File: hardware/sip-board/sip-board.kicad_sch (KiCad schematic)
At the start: 85 parts, among them IC1 XC7S15-1CPGA196C, J1 Conn_01x06_Pin, J2 Conn_01x10_Pin, J3 Conn_01x10_Pin, J4 Conn_01x10_Pin, J5 Conn_01x10_Pin, SW2 SW_RESET, U1 TLV75718PDRV, U2 TLV75733PDRV, U3 TLV75710PDRV

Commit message: add new spi chip supported by vivado
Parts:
- removed D1: D_Small, Diode_SMD:D_0201_0603Metric, symbol Device:D_Small
- removed J1: Conn_01x06_Pin, Connector_PinHeader_2.54mm:PinHeader_1x06_P2.54mm_Vertical_SMD_Pin1Left, symbol Connector:Conn_01x06_Pin
- removed R15: 2k4, Resistor_SMD:R_0201_0603Metric, symbol Device:R_Small
- removed SPIPROM1: M95256-WMN6P, Package_SO:SOIC-8_3.9x4.9mm_P1.27mm, symbol Memory_EEPROM:M95256-WMN6P
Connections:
- net A0_FPGA: no longer IC1.F13 (IO_L11N_T1_SRCC_14)
- net A10_FPGA: no longer IC1.N13 (IO_L20P_T3_D24_14)
- net A11_FPGA: no longer IC1.B1 (IO_L5N_T0_34)
- net A12_FPGA: no longer IC1.C1 (IO_L7N_T1_34)
- net A13_FPGA: no longer IC1.D1 (IO_L9N_T1_DQS_34)
- net A14_FPGA: no longer IC1.E1 (IO_L9P_T1_DQS_34)
- net A15_FPGA: no longer IC1.G1 (IO_L12N_T1_MRCC_34)
- net A1_FPGA: no longer IC1.F14 (IO_L12N_T1_MRCC_14)
- net A2_FPGA: no longer IC1.G14 (IO_L12P_T1_MRCC_14)
- net A3_FPGA: no longer IC1.H13 (IO_L14N_T2_SRCC_14)
- net A4_FPGA: no longer IC1.H14 (IO_L15N_T2_DQS_DOUT_CSO_B_14)
- net A5_FPGA: no longer IC1.J13 (IO_L14P_T2_SRCC_14)
- net A6_FPGA: no longer IC1.J14 (IO_L15P_T2_DQS_RDWR_B_14)
- net A7_FPGA: no longer IC1.L14 (IO_L17N_T2_D29_14)
- net A8_FPGA: no longer IC1.M14 (IO_L17P_T2_D30_14)
- net A9_FPGA: no longer IC1.N14 (IO_L20N_T3_D23_14)
- net BUSAK_FPGA: no longer IC1.C12 (IO_L5P_T0_D06_14)
- net BUSRQ_FPGA: no longer IC1.B14 (IO_L7N_T1_D10_14)
- net CLK: now also IC1.H4 (IO_L13P_T2_MRCC_34); no longer IC1.H1 (IO_L15N_T2_DQS_34)
- net D0_FPGA: no longer IC1.K3 (IO_L18P_T2_34)
- net D1_FPGA: no longer IC1.L2 (IO_L17P_T2_34)
- net D2_FPGA: no longer IC1.M1 (IO_L20N_T3_34)
- net D3_FPGA: no longer IC1.J1 (IO_L15P_T2_DQS_34)
- net D4_FPGA: no longer IC1.K1 (IO_L17N_T2_34)
- net D5_FPGA: no longer IC1.N1 (IO_L21N_T3_DQS_34)
- net D6_FPGA: no longer IC1.M2 (IO_L20P_T3_34)
- net D7_FPGA: no longer IC1.K2 (IO_L18N_T2_34)
- net DONE: no longer IC1.M9 (DONE_0)
- net HALT_FPGA: no longer IC1.N4 (IO_L24P_T3_34)
- net INT_FPGA: no longer IC1.L4 (IO_L19P_T3_34)
- net IORQ_FPGA: no longer IC1.P4 (IO_L22P_T3_34)
- net M1_FPGA: no longer IC1.D14 (IO_L8N_T1_D12_14)
- net MREQ_FPGA: no longer IC1.P3 (IO_L23P_T3_34)
- net NMI_FPGA: no longer IC1.N3 (IO_L22N_T3_34)
- net RD_FPGA: no longer IC1.A12 (IO_L2N_T0_D03_14)
- net RESET_FPGA: no longer IC1.C14 (IO_L7P_T1_D09_14)
- net RFSH_FPGA: no longer IC1.E13 (IO_L8P_T1_D11_14)
- net WAIT_FPGA: no longer IC1.A13 (IO_0_14)
- net WR_FPGA: no longer IC1.B12 (IO_L5N_T0_D07_14)
- net CCLK: no longer names the net of IC1.A7 (CCLK_0)
- net CCLK: no longer IC1.A8 (TCK_0)
- net CS: no longer names the net of IC1.D13 (IO_L6P_T0_FCS_B_14)
- net CS: no longer IC1.L7 (TMS_0)
- net DIN: no longer names the net of IC1.C11 (IO_L1N_T0_D01_DIN_14)
- net MOSI: no longer names the net of IC1.C10 (IO_L1P_T0_D00_MOSI_14)
- net MOSI: no longer IC1.M7 (TDI_0)
- net TDO: no longer names the net of IC1.M6 (TDO_0)
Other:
- note added: "Choosing is25lp016d for now; cheap, high density, qspi, directly supported by Vivado"
- note added: "M[2:0] = 001 for Master SPI config"
- note added: "`CLK` signal is routed into H4 (MRCC) as it can be used in global clock tree this must be configured in the constraints file"
- note added: "https://docs.amd.com/r/en-US/xapp586-spi-flash/SPI-Flash-Configuration-Interface https://docs.amd.com/r/2021.2-English/ug908-vivado-programming-debugging/Spartan-7-Configuration-Memory-Devices"
- note removed: "JTAG <-> SPI Thank you digilent. I love you. JTAG-HS1 Connector Note: DO NOT connect both JTAG and Z80 board at same time."
- note removed: "SPI PROM 3.9mm x 4.9mm We are configuring FPGA from SPI - see Config UG"
- moved on the sheet: J2, J3, J4, J5, R10, R11, R12, R13, R4, R5, R6, R7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

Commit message: 3d model for fpga, part placement done(?)
Look into Xilinx programming adapters still. We do not have lots of space to work with.
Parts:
- added J1: Conn_01x05_Pin, Connector_PinHeader_2.54mm:PinHeader_1x05_P2.54mm_Vertical, symbol Connector:Conn_01x05_Pin
- added U15: AT25SF081-XMHD-X, Package_SO:TSSOP-8_4.4x3mm_P0.65mm, symbol Memory_Flash:AT25SF081-XMHD-X
- C10, C12, C13, C16, C17, C18, C19, C20, C21, C22, C23, C26, C27, C28, C29, C30, C31, C32, C33, C34, C36, C37, C7, C8, C9: footprint Capacitor_SMD:C_0201_0603Metric -> Capacitor_SMD:C_01005_0402Metric
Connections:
- net +3V3: now also J1.1 (Pin_1), U15.8 (VCC)
- net A0_5V: now also J4.1 (Pin_1), U12.9 (B3); no longer J4.10 (Pin_10), U12.10 (B2)
- net A0_FPGA: now also U12.4 (A3); no longer U12.3 (A2)
- net A10_5V: now also J5.1 (Pin_1), U14.11 (B1); no longer J5.10 (Pin_10), U14.8 (B4)
- net A10_FPGA: now also U14.2 (A1); no longer U14.5 (A4)
- net A1_5V: now also J5.10 (Pin_10), U12.10 (B2); no longer J5.1 (Pin_1), U12.9 (B3)
- net A1_FPGA: now also U12.3 (A2); no longer U12.4 (A3)
- net A2_5V: now also J5.9 (Pin_9), U12.11 (B1); no longer J5.2 (Pin_2), U12.8 (B4)
- net A2_FPGA: now also U12.2 (A1); no longer U12.5 (A4)
- net A3_5V: now also J5.8 (Pin_8), U13.8 (B4); no longer J5.3 (Pin_3), U13.11 (B1)
- net A3_FPGA: now also U13.5 (A4); no longer U13.2 (A1)
- net A4_5V: now also J5.7 (Pin_7), U13.9 (B3); no longer J5.4 (Pin_4), U13.10 (B2)
- net A4_FPGA: now also U13.4 (A3); no longer U13.3 (A2)
- net A5_5V: now also J5.6 (Pin_6), U13.10 (B2); no longer J5.5 (Pin_5), U13.9 (B3)
- net A5_FPGA: now also U13.3 (A2); no longer U13.4 (A3)
- net A6_5V: now also J5.5 (Pin_5), U13.11 (B1); no longer J5.6 (Pin_6), U13.8 (B4)
- net A6_FPGA: now also U13.2 (A1); no longer U13.5 (A4)
- net A7_5V: now also J5.4 (Pin_4), U14.8 (B4); no longer J5.7 (Pin_7), U14.11 (B1)
- net A7_FPGA: now also U14.5 (A4); no longer U14.2 (A1)
- net A8_5V: now also J5.3 (Pin_3), U14.9 (B3); no longer J5.8 (Pin_8), U14.10 (B2)
- net A8_FPGA: now also U14.4 (A3); no longer U14.3 (A2)
- net A9_5V: now also J5.2 (Pin_2), U14.10 (B2); no longer J5.9 (Pin_9), U14.9 (B3)
- net A9_FPGA: now also U14.3 (A2); no longer U14.4 (A3)
- net BUSAK_5V: now also J4.8 (Pin_8), U10.10 (B2); no longer J4.3 (Pin_3), U10.9 (B3)
- net BUSAK_FPGA: now also U10.3 (A2); no longer U10.4 (A3)
- net BUSRQ_5V: now also J4.6 (Pin_6), U11.8 (B4); no longer J4.5 (Pin_5), U11.11 (B1)
- net BUSRQ_FPGA: now also U11.5 (A4); no longer U11.2 (A1)
- net DONE: now also IC1.M9 (DONE_0)
- net GND: now also J4.2 (Pin_2), U15.4 (GND); no longer J4.9 (Pin_9)
- net M1_5V: now also J4.4 (Pin_4), U11.10 (B2); no longer J4.7 (Pin_7), U11.9 (B3)
- net M1_FPGA: now also U11.3 (A2); no longer U11.4 (A3)
- net RD_5V: now also J4.10 (Pin_10), U10.8 (B4); no longer J4.1 (Pin_1), U10.11 (B1)
- net RD_FPGA: now also U10.5 (A4); no longer U10.2 (A1)
- net RESET_5V: now also J4.5 (Pin_5), U11.9 (B3); no longer J4.6 (Pin_6), U11.10 (B2)
- net RESET_FPGA: now also U11.4 (A3); no longer U11.3 (A2)
- net RFSH_5V: now also J4.3 (Pin_3), U11.11 (B1); no longer J4.8 (Pin_8), U11.8 (B4)
- net RFSH_FPGA: now also U11.2 (A1); no longer U11.5 (A4)
- net WAIT_5V: now also J4.7 (Pin_7), U10.11 (B1); no longer J4.4 (Pin_4), U10.8 (B4)
- net WAIT_FPGA: now also U10.2 (A1); no longer U10.5 (A4)
- net WR_5V: now also J4.9 (Pin_9), U10.9 (B3); no longer J4.2 (Pin_2), U10.10 (B2)
- net WR_FPGA: now also U10.4 (A3); no longer U10.3 (A2)
- net SPI_DQ3: now reaches IC1.A12 (IO_L2N_T0_D03_14)
- net SPI_DQ3: now also U15.7 (~{HOLD}/IO3)
- net SPI_SCK: now reaches IC1.A7 (CCLK_0)
- net SPI_SCK: now also U15.6 (SCK)
- net JTAG_TCK: now reaches IC1.A8 (TCK_0)
- net JTAG_TCK: now also J1.2 (Pin_2)
- net SPI_DQ2: now reaches IC1.B11 (IO_L2P_T0_D02_14)
- net SPI_DQ2: now also U15.3 (~{WP}/IO2)
- net SPI_DQ0: now reaches IC1.C10 (IO_L1P_T0_D00_MOSI_14)
- net SPI_DQ0: now also U15.5 (SI/IO0)
- net SPI_DQ1: now reaches IC1.C11 (IO_L1N_T0_D01_DIN_14)
- net SPI_DQ1: now also U15.2 (SO/IO1)
- net SPI_CS: now reaches IC1.D13 (IO_L6P_T0_FCS_B_14)
- net SPI_CS: now also U15.1 (~{CS})
- net JTAG_TMS: now reaches IC1.L7 (TMS_0)
- net JTAG_TMS: now also J1.3 (Pin_3)
- net JTAG_TDO: now reaches IC1.M6 (TDO_0)
- net JTAG_TDO: now also J1.5 (Pin_5)
- net JTAG_TDI: now reaches IC1.M7 (TDI_0)
- net JTAG_TDI: now also J1.4 (Pin_4)
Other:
- note added: "Configuration Banks Voltage Select section in the config user guide; tldr we are running of 3v3 for SPI flash so this needs to be pulled up to 3v3 as well"
- note added: "SPI Memory"
- note added: "The Xilinx connector is actually a 2x7 connector, but half the pins are ground, 4 of the pins are real JTAG signals, 1 is power, and 2 are NC."
- note added: "This A4 pin --> is GND on original Z80"
- note added: "This chip is not directly supported by Vivado for flash programming. We need to determine if it works identically to the supported chips or if we have to configure Vivado for it"
- note added: "Xilinx JTAG connector"
- note added: "Xilinx recommends specific power on sequence for each LDO, but I haven't found small enough LDOs with enable pins, so we're scaling up the capacitor values for now. Fix!"
- note removed: "Choosing is25lp016d for now; cheap, high density, qspi, directly supported by Vivado"
- note removed: "Configuration Banks Voltage Select section in the config user guide"
- note removed: "This A1 --> is GND on original Z80"

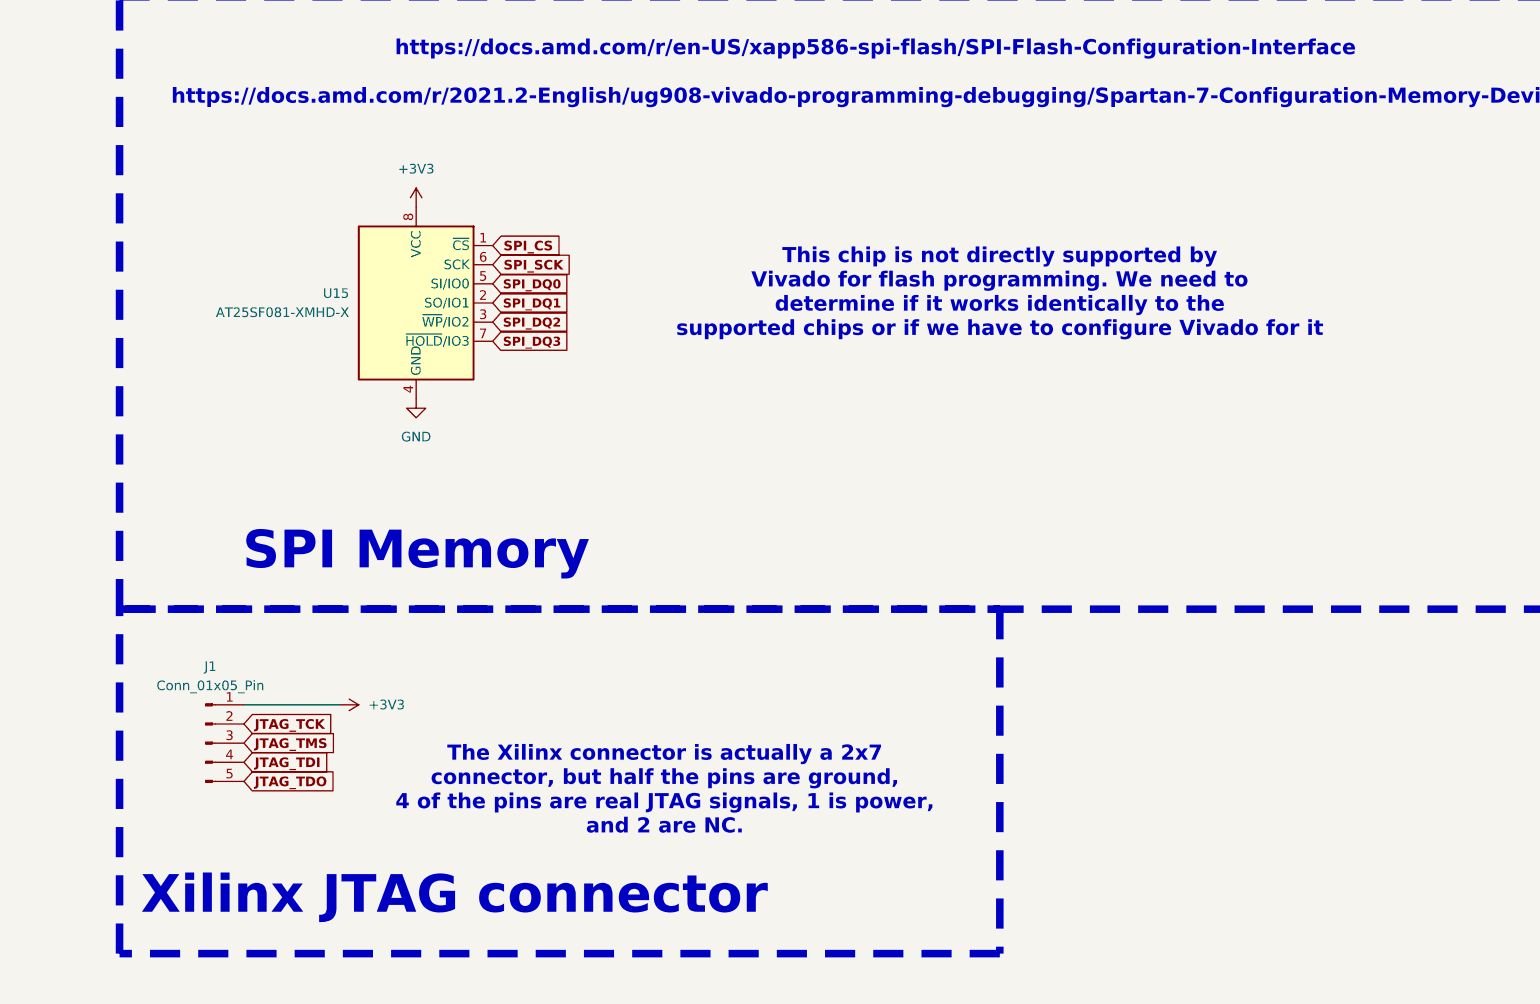
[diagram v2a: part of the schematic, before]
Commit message: update to use relative paths
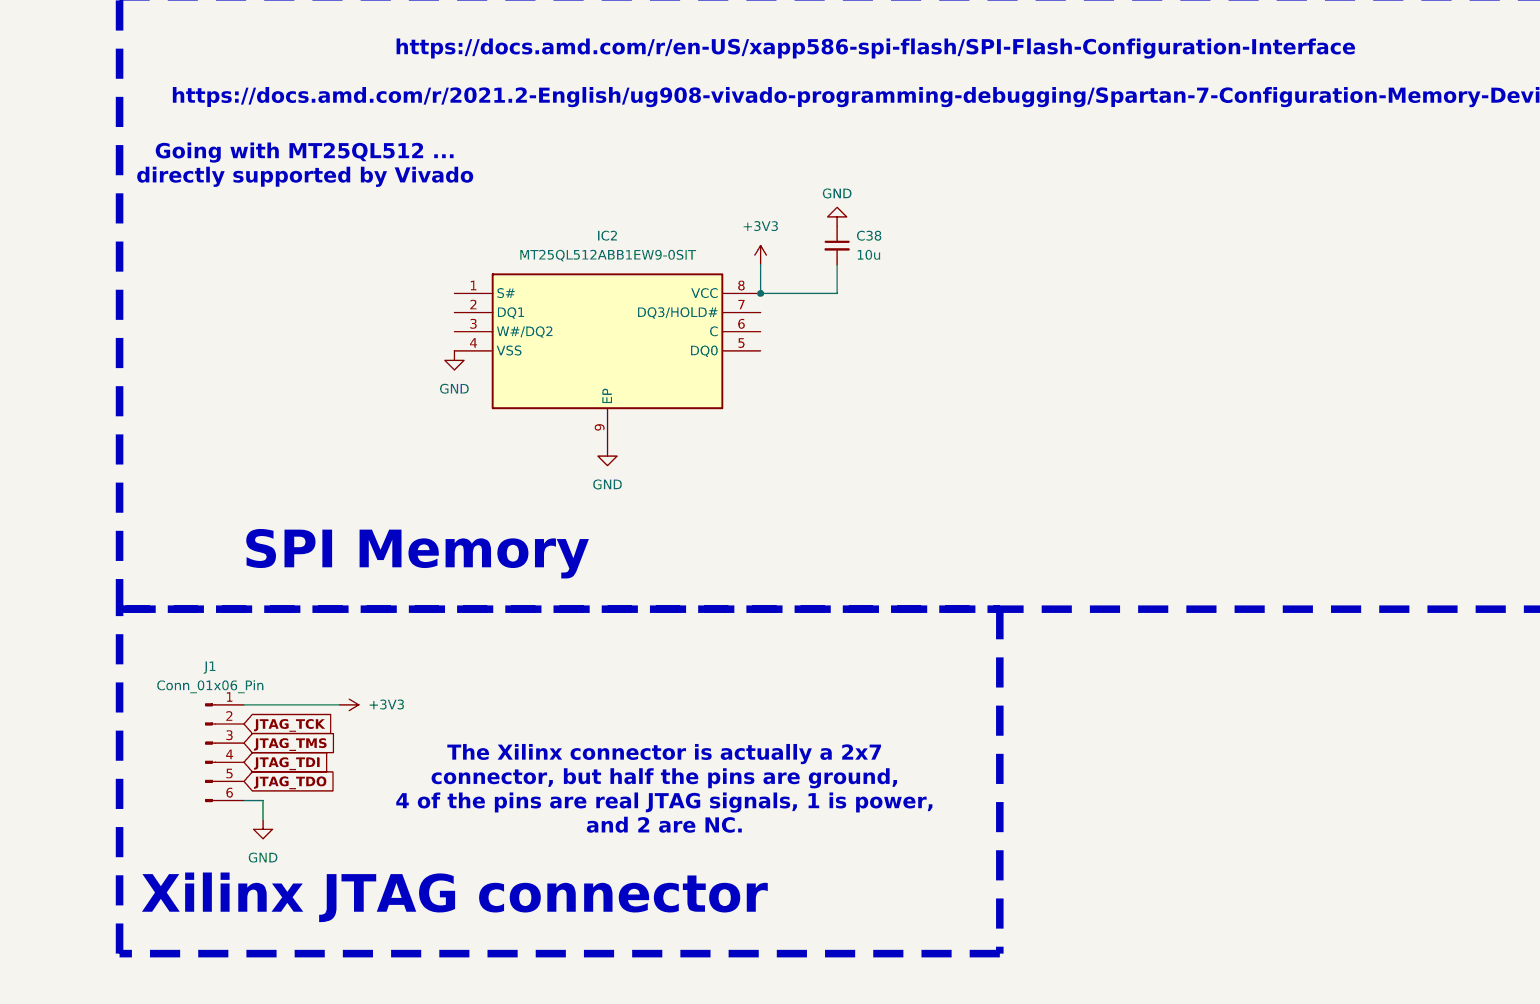
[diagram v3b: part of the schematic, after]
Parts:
- removed J1: Conn_01x05_Pin, Connector_PinHeader_2.54mm:PinHeader_1x05_P2.54mm_Vertical, symbol Connector:Conn_01x05_Pin
- removed U15: AT25SF081-XMHD-X, Package_SO:TSSOP-8_4.4x3mm_P0.65mm, symbol Memory_Flash:AT25SF081-XMHD-X
- added C38: 10u, symbol Device:C_Small
- added IC2: MT25QL512ABB1EW9-0SIT, SON127P800X600X80-9N-D, symbol MT25QL512ABB1EW9-0SIT:MT25QL512ABB1EW9-0SIT
- added J1: Conn_01x06_Pin, symbol Connector:Conn_01x06_Pin
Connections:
- net +3V3: now also C38.2, IC2.8 (VCC), J1.1 (Pin_1)
- net GND: now also C38.1, IC2.4 (VSS), IC2.9 (EP), J1.6 (Pin_6)
- net JTAG_TCK: now also J1.2 (Pin_2)
- net JTAG_TDI: now also J1.4 (Pin_4)
- net JTAG_TDO: now also J1.5 (Pin_5)
- net JTAG_TMS: now also J1.3 (Pin_3)
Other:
- note added: "Going with MT25QL512 ... directly supported by Vivado"
- note removed: "This chip is not directly supported by Vivado for flash programming. We need to determine if it works identically to the supported chips or if we have to configure Vivado for it"

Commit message: fix the paths (again)
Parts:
- added R15, R21: 5k, Resistor_SMD:R_0201_0603Metric, symbol Device:R_Small
- C1, C14, C15, C2, C25, C3, C5: footprint Capacitor_SMD:C_0201_0603Metric -> Capacitor_SMD:C_0402_1005Metric
- C10, C12, C13, C16, C17, C18, C19, C20, C21, C22, C23, C26, C27, C28, C29, C30, C31, C32, C33, C34, C36, C37, C7, C8, C9: footprint Capacitor_SMD:C_01005_0402Metric -> Capacitor_SMD:C_0201_0603Metric
- C38: footprint (none) -> Capacitor_SMD:C_0402_1005Metric
- IC2: footprint SON127P800X600X80-9N-D -> hardware:MT25QL512ABB1EW9-0SIT
- JTAG1: renamed from J1; footprint (none) -> Connector_PinHeader_2.54mm:PinHeader_1x06_P2.54mm_Vertical
- U10, U11, U12, U13, U14, U5, U6, U7, U8, U9: footprint hardware:NXB0104_XQFN12 -> hardware:NXB0104GU12X
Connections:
- net +3V3: now also R15.1, R21.1
- net SPI_CS: now also IC2.1 (S#), R15.2
- net SPI_DQ0: now also IC2.5 (DQ0), IC2.7 (DQ3/HOLD#)
- net SPI_DQ1: now also IC2.2 (DQ1)
- net SPI_DQ2: now also IC2.3 (W#/DQ2), R21.2
- net SPI_SCK: now also IC2.6 (C)
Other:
- note added: "Per datasheet, W# must be pulled high to enable writes, regardless of current mode"

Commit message: add new parts: button, jtag connector
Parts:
- removed INIT1: LED, LED_SMD:LED_0201_0603Metric, symbol Device:LED
- removed JTAG1: Conn_01x06_Pin, Connector_PinHeader_2.54mm:PinHeader_1x06_P2.54mm_Vertical, symbol Connector:Conn_01x06_Pin
- removed SW2: SW_RESET, Button_Switch_SMD:SW_Push_1P1T_NO_6x6mm_H9.5mm, symbol Switch:SW_Push
- added J1: Conn_02x03_Odd_Even, hardware:TAG_TC2030-IDC-NL, symbol Connector_Generic:Conn_02x03_Odd_Even
- added S1: EVQ-P2R02W, hardware:EVQP2R02W, symbol EVQ-P2R02W:EVQ-P2R02W
- added TP1, TP2, TP3, TP4, TP5, TP6, TP7: TestPoint, TestPoint:TestPoint_Pad_1.0x1.0mm, symbol Connector:TestPoint
- R14, R15, R21: value 5k -> 4k7
- R17: value 5k7 -> 4k7
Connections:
- net +3V3: now also IC1.B10 (IO_L3P_T0_DQS_PUDC_B_14), R16.1, R17.1, J1.1 (Pin_1)
- net DONE: now also DONE1.2 (A); no longer R17.1
- net GND: now also J1.5 (Pin_5); no longer IC1.B10 (IO_L3P_T0_DQS_PUDC_B_14)
- net JTAG_TCK: now also J1.4 (Pin_4)
- net JTAG_TDI: now also J1.3 (Pin_3)
- net JTAG_TDO: now also J1.6 (Pin_6)
- net JTAG_TMS: now also J1.2 (Pin_2)
- net PROGRAM_B: now also S1.2 (COM_1)
- net SPI_CS: now also TP3.1
- net SPI_DQ0: now also TP4.1; no longer IC2.7 (DQ3/HOLD#)
- net SPI_DQ1: now also TP5.1
- net SPI_DQ2: now also TP6.1
- net SPI_DQ3: now also IC2.7 (DQ3/HOLD#), R17.2, TP7.1
- net INIT_B: now reaches IC1.N7 (INIT_B_0), R16.2
- net INIT_B: now also TP1.1
- net at C11.1: now also S1.4 (COM_2), S1.5 (GND)
- net SPI_SCK renamed SPI_SCK_CCLK
- net SPI_SCK_CCLK: now also TP2.1
- no-connect marks 16 -> 18
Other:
- note added: "Configuration Banks Voltage Select section in the config user guide; tldr we are running of 3v3 for SPI flash so CFGBVS needs to be 3v3 as well"
- note added: "DONE"
- note added: "INIT"
- note added: "JTAG Connector"
- note added: "Per datasheet, W# must be pulled high initially to enable writes, regardless of current mode"
- note added: "SPI testpoints"
- note added: "Status LEDs/test points"
- note added: "The DONE pin has an internal 10k pull-up resistor. It is pulled high when config is finished."
- note added: "UG470 7-Series pg.25"
- note added: "UG470 pg 22"
- note added: "UG470 pg27 Need pull-ups on DQ2/3, CS"
- note added: "We aren't daisy chaining any JTAG pins, so we don't need pull-ups, per UG470"
- note added: "When pulled high the FPGA proceeds with configured initialization per M[2:0] pins. Expose a test pad here"
- note added: "https://www.tag-connect.com/wp-content/uploads/bsk-pdf-manager/2019/12/TC2030-IDC-NL-Datasheet-Rev-B.pdf"
- note removed: "Configuration Banks Voltage Select section in the config user guide; tldr we are running of 3v3 for SPI flash so this needs to be pulled up to 3v3 as well"
- note removed: "Per datasheet, W# must be pulled high to enable writes, regardless of current mode"
- note removed: "The Xilinx connector is actually a 2x7 connector, but half the pins are ground, 4 of the pins are real JTAG signals, 1 is power, and 2 are NC."
- note removed: "Xilinx JTAG connector"
- moved on the sheet: C11, DONE1, R16
